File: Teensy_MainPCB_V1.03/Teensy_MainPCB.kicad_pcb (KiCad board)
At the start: 2 copper layers, 141.9 x 100 mm, 62 parts, among them J1 ODO_Right, J10 Sonar_R, J11 Cutter, J12 Sonar_L, J13 P_Right, J15 Button, J16 Power_PCB1, J17 Power_PCB2, J18 Free01_02, J19 P_Left, J2 I2C2_0, J20 Can3, J21 Ser5, J22 FreeA16_A17, J23 ESP RFID1, J24 ESP RFID2, J25 5V IN, J26 ESP32 I2C, J27 ESP32 Sens1, J28 ESP32 FREE, J3 I2C0_0, J30 I2C1_0, J31 Ser3, J32 ESP32 Sens2, J33 ESP32 I2C/SER, J34 Teensy On/Off, J4 I2C1_1, J5 Bumper, J6 ODO_Left, J7 Motor_Right1, J8 Motor_Left1, J9 Rain, U2 GY-521, U3 Teensy4.1, U4 ESP32-DEVKIT-V1

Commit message: v1.03
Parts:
- removed D7: 1N5819, Diode_THT:D_DO-41_SOD81_P10.16mm_Horizontal
- removed J32: ESP32 Sens2, Connector_JST:JST_XH_B3B-XH-A_1x03_P2.50mm_Vertical
- removed J33: ESP32 I2C/SER, Connector_JST:JST_XH_B4B-XH-A_1x04_P2.50mm_Vertical
- removed J34: Teensy On/Off, Connector_JST:JST_XH_B2B-XH-A_1x02_P2.50mm_Vertical
- removed JP3: MotorPower, Connector_PinHeader_2.54mm:PinHeader_1x03_P2.54mm_Vertical
- removed JP5: CutterPower, Connector_PinHeader_2.54mm:PinHeader_1x03_P2.54mm_Vertical
- removed U4: ESP32-DEVKIT-V1, teensy_library-master:ESP32-DEVKIT-V1
- added C1: CP1, Capacitor_THT:CP_Radial_D8.0mm_P3.80mm, F.Cu at (53.5, 119.2)
- added D1: 1N4733A, Diode_THT:D_DO-41_SOD81_P10.16mm_Horizontal, F.Cu at (51.1, 47.1)
- added J14: Button, Connector_JST:JST_XH_B2B-XH-A_1x02_P2.50mm_Vertical, F.Cu at (43.5, 122.4)
- added J29: ESP RFID2, Connector_JST:JST_XH_B5B-XH-A_1x05_P2.50mm_Vertical, F.Cu at (119.7, 117.1)
- added JP1: MotorPower, Connector_PinHeader_2.54mm:PinHeader_1x03_P2.54mm_Vertical, F.Cu at (171.0, 121.7)
- added JP2: CutterPower, Connector_PinHeader_2.54mm:PinHeader_1x03_P2.54mm_Vertical, F.Cu at (171.6, 49.0)
- added R11: XXXX, Resistor_THT:R_Axial_DIN0207_L6.3mm_D2.5mm_P2.54mm_Vertical, F.Cu at (55.5, 38.8)
- added U1: Teensy4.1, teensy_library-master:Teensy41, F.Cu at (69.0, 87.7)
- added kibuzzard-62AA1DDF: G***, kibuzzard-62AA1DDF, F.Cu at (39.4, 111.8)
- added kibuzzard-62AA1E85: G***, kibuzzard-62AA1E85, F.Cu at (53.4, 80.6)
- added kibuzzard-62AA1F05: G***, kibuzzard-62AA1F05, F.Cu at (53.1, 83.2)
- added kibuzzard-62AA3447: G***, kibuzzard-62AA3447, F.Cu at (68.7, 42.2)
- added kibuzzard-62AA347B: G***, kibuzzard-62AA347B, F.Cu at (50.2, 95.9)
- added kibuzzard-62AA34D8: G***, kibuzzard-62AA34D8, F.Cu at (50.2, 98.3)
- added kibuzzard-62AA353C: G***, kibuzzard-62AA353C, F.Cu at (50.2, 100.7)
- added kibuzzard-62AA3566: G***, kibuzzard-62AA3566, F.Cu at (50.2, 103.3)
- added kibuzzard-62AA39DC: G***, kibuzzard-62AA39DC, F.Cu at (39.5, 120.9)
- added kibuzzard-62AA3A43: G***, kibuzzard-62AA3A43, F.Cu at (39.5, 97.2)
- added kibuzzard-62AA3A85: G***, kibuzzard-62AA3A85, F.Cu at (39.4, 81.9)
- added kibuzzard-62AA3B12: G***, kibuzzard-62AA3B12, F.Cu at (39.4, 48.0)
- added kibuzzard-62AB5E06: G***, kibuzzard-62AB5E06, F.Cu at (81.3, 35.6)
- added kibuzzard-62AB5E66: G***, kibuzzard-62AB5E66, F.Cu at (63.0, 35.6)
- added kibuzzard-62AB5ED1: G***, kibuzzard-62AB5ED1, F.Cu at (93.6, 35.6)
- added kibuzzard-62AB5F2F: G***, kibuzzard-62AB5F2F, F.Cu at (102.0, 35.6)
- added kibuzzard-62AB5F67: G***, kibuzzard-62AB5F67, F.Cu at (114.3, 35.6)
- added kibuzzard-62AB5FC4: G***, kibuzzard-62AB5FC4, F.Cu at (129.3, 35.5)
- added kibuzzard-62AB5FF2: G***, kibuzzard-62AB5FF2, F.Cu at (137.7, 35.5)
- added kibuzzard-62AB6021: G***, kibuzzard-62AB6021, F.Cu at (150.9, 35.5)
- added kibuzzard-62AB60B1: G***, kibuzzard-62AB60B1, F.Cu at (90.7, 62.4)
- added kibuzzard-62AB6109: G***, kibuzzard-62AB6109, F.Cu at (90.6, 65.0)
- added kibuzzard-62AB62B6: G***, kibuzzard-62AB62B6, F.Cu at (87.4, 44.7)
- added kibuzzard-62AB62D3: G***, kibuzzard-62AB62D3, F.Cu at (87.5, 47.3)
- added kibuzzard-62AB634F: G***, kibuzzard-62AB634F, F.Cu at (108.2, 44.9)
- added kibuzzard-62AB6374: G***, kibuzzard-62AB6374, F.Cu at (108.2, 47.5)
- added kibuzzard-62AB639B: G***, kibuzzard-62AB639B, F.Cu at (121.8, 44.8)
- added kibuzzard-62AB63D2: G***, kibuzzard-62AB63D2, F.Cu at (121.6, 47.4)
- added kibuzzard-62AB64C2: G***, kibuzzard-62AB64C2, F.Cu at (144.3, 42.2)
- added kibuzzard-62AB64F2: G***, kibuzzard-62AB64F2, F.Cu at (143.9, 47.3)
- added kibuzzard-62AB6557: G***, kibuzzard-62AB6557, F.Cu at (156.3, 44.6)
- added kibuzzard-62AB6A77: G***, kibuzzard-62AB6A77, F.Cu at (84.6, 55.9)
- added kibuzzard-62AB6A93: G***, kibuzzard-62AB6A93, F.Cu at (97.0, 55.8)
- added kibuzzard-62AB6AFA: G***, kibuzzard-62AB6AFA, F.Cu at (90.3, 67.5)
- added kibuzzard-62AB6B3D: G***, kibuzzard-62AB6B3D, F.Cu at (90.3, 70.0)
- added kibuzzard-62AB6B9B: G***, kibuzzard-62AB6B9B, F.Cu at (102.6, 70.0)
- added kibuzzard-62AB6BA8: G***, kibuzzard-62AB6BA8, F.Cu at (102.6, 67.5)
- added kibuzzard-62AB6BF4: G***, kibuzzard-62AB6BF4, F.Cu at (111.6, 55.7)
- added kibuzzard-62AB6CC8: G***, kibuzzard-62AB6CC8, F.Cu at (123.6, 55.6)
- added kibuzzard-62AB6D7A: G***, kibuzzard-62AB6D7A, F.Cu at (114.2, 65.6)
- added kibuzzard-62AB6EF0: G***, kibuzzard-62AB6EF0, F.Cu at (139.4, 55.6)
- added kibuzzard-62AB6F91: G***, kibuzzard-62AB6F91, F.Cu at (142.9, 66.2)
- added kibuzzard-62AB7031: G***, kibuzzard-62AB7031, F.Cu at (174.2, 46.1)
- added kibuzzard-62AB756D: G***, kibuzzard-62AB756D, F.Cu at (154.6, 55.5)
- added kibuzzard-62AB767F: G***, kibuzzard-62AB767F, F.Cu at (173.5, 118.8)
- added kibuzzard-62AB774A: G***, kibuzzard-62AB774A, F.Cu at (167.0, 69.5)
- added kibuzzard-62AB778D: G***, kibuzzard-62AB778D, F.Cu at (178.2, 63.4)
- added kibuzzard-62AB77E5: G***, kibuzzard-62AB77E5, F.Cu at (178.1, 84.4)
- added kibuzzard-62AB789F: G***, kibuzzard-62AB789F, F.Cu at (177.9, 106.4)
- added kibuzzard-62AC4CEE: G***, kibuzzard-62AC4CEE, F.Cu at (153.4, 98.2)
- added kibuzzard-62AC4D6D: G***, kibuzzard-62AC4D6D, F.Cu at (155.7, 88.1)
- added kibuzzard-62AC52F4: G***, kibuzzard-62AC52F4, F.Cu at (96.0, 132.2)
- added kibuzzard-62AC8CBD: G***, kibuzzard-62AC8CBD, F.Cu at (143.4, 39.7)
- added kibuzzard-62AC8CC8: G***, kibuzzard-62AC8CC8, F.Cu at (143.5, 44.9)
- added kibuzzard-62AC8CD7: G***, kibuzzard-62AC8CD7, F.Cu at (156.8, 42.3)
- added kibuzzard-62AC8CE7: G***, kibuzzard-62AC8CE7, F.Cu at (111.6, 66.1)
- added kibuzzard-62AC8CFB: G***, kibuzzard-62AC8CFB, F.Cu at (123.6, 66.1)
- added kibuzzard-62AC8D10: G***, kibuzzard-62AC8D10, F.Cu at (140.3, 66.1)
- added kibuzzard-62AC8D1B: G***, kibuzzard-62AC8D1B, F.Cu at (155.8, 66.1)
- added kibuzzard-62AC8D87: G***, kibuzzard-62AC8D87, F.Cu at (153.2, 88.0)
- added kibuzzard-62AC8DAF: G***, kibuzzard-62AC8DAF, F.Cu at (49.8, 122.8)
- added kibuzzard-62AC8DEE: G***, kibuzzard-62AC8DEE, F.Cu at (50.1, 90.7)
- added kibuzzard-62AC8E7D: G***, kibuzzard-62AC8E7D, F.Cu at (108.1, 42.3)
- added kibuzzard-62AC8E96: G***, kibuzzard-62AC8E96, F.Cu at (121.6, 42.1)
- added kibuzzard-62AC8EE6: G***, kibuzzard-62AC8EE6, F.Cu at (90.7, 59.9)
- added kibuzzard-62AC8F0E: G***, kibuzzard-62AC8F0E, F.Cu at (121.0, 65.6)
- added kibuzzard-62AC8F57: G***, kibuzzard-62AC8F57, F.Cu at (158.3, 66.3)
- added kibuzzard-62AC8F80: G***, kibuzzard-62AC8F80, F.Cu at (135.3, 66.5)
- added kibuzzard-62AC8F92: G***, kibuzzard-62AC8F92, F.Cu at (150.9, 66.6)
- added kibuzzard-62AC8FB5: G***, kibuzzard-62AC8FB5, F.Cu at (126.1, 65.8)
- added kibuzzard-62AC8FDD: G***, kibuzzard-62AC8FDD, F.Cu at (137.8, 65.7)
- added kibuzzard-62AC8FEE: G***, kibuzzard-62AC8FEE, F.Cu at (153.3, 65.8)
- added kibuzzard-62AC90B9: G***, kibuzzard-62AC90B9, F.Cu at (150.7, 87.6)
- added kibuzzard-62AC90FB: G***, kibuzzard-62AC90FB, F.Cu at (69.1, 39.6)
- added kibuzzard-62AC9112: G***, kibuzzard-62AC9112, F.Cu at (157.2, 39.7)
- added kibuzzard-62AC9161: G***, kibuzzard-62AC9161, F.Cu at (167.8, 62.0)
- added kibuzzard-62AC916E: G***, kibuzzard-62AC916E, F.Cu at (167.7, 83.1)
- added kibuzzard-62AC917A: G***, kibuzzard-62AC917A, F.Cu at (167.6, 105.0)
- added kibuzzard-62AC918B: G***, kibuzzard-62AC918B, F.Cu at (167.7, 64.5)
- added kibuzzard-62AC9196: G***, kibuzzard-62AC9196, F.Cu at (167.7, 85.8)
- added kibuzzard-62AC91A3: G***, kibuzzard-62AC91A3, F.Cu at (167.5, 107.6)
- added kibuzzard-62AC91BB: G***, kibuzzard-62AC91BB, F.Cu at (168.2, 67.0)
- added kibuzzard-62AC91C5: G***, kibuzzard-62AC91C5, F.Cu at (168.1, 88.3)
- added kibuzzard-62AC91DF: G***, kibuzzard-62AC91DF, F.Cu at (167.9, 110.1)
- added kibuzzard-62AC91F0: G***, kibuzzard-62AC91F0, F.Cu at (166.7, 112.6)
- added kibuzzard-62AC9203: G***, kibuzzard-62AC9203, F.Cu at (166.7, 90.8)
- added kibuzzard-62AC92C8: G***, kibuzzard-62AC92C8, F.Cu at (49.8, 93.4)
- added kibuzzard-62AC9315: G***, kibuzzard-62AC9315, F.Cu at (69.0, 44.9)
- added kibuzzard-62AC932E: G***, kibuzzard-62AC932E, F.Cu at (69.1, 47.4)
- added kibuzzard-62AC9376: G***, kibuzzard-62AC9376, F.Cu at (109.0, 65.7)
- added kibuzzard-62AC93D0: G***, kibuzzard-62AC93D0, F.Cu at (87.6, 42.3)
- added kibuzzard-62AC95A7: G***, kibuzzard-62AC95A7, F.Cu at (167.6, 59.3)
- added kibuzzard-62AC95BD: G***, kibuzzard-62AC95BD, F.Cu at (167.6, 80.6)
- added kibuzzard-62AC95C9: G***, kibuzzard-62AC95C9, F.Cu at (167.5, 102.5)
- added kibuzzard-62AC961B: G***, kibuzzard-62AC961B, F.Cu at (87.5, 39.7)
- added kibuzzard-62AC9630: G***, kibuzzard-62AC9630, F.Cu at (108.2, 39.9)
- added kibuzzard-62AC9639: G***, kibuzzard-62AC9639, F.Cu at (121.6, 39.6)
- J1: value ODO_Right -> 5V IN; footprint Connector_JST:JST_XH_B4B-XH-A_1x04_P2.50mm_Vertical -> TerminalBlock:TerminalBlock_bornier-2_P5.08mm
- J10: value Sonar_R -> P_Right; footprint Connector_JST:JST_XH_B4B-XH-A_1x04_P2.50mm_Vertical -> Connector_JST:JST_XH_B3B-XH-A_1x03_P2.50mm_Vertical
- J11: value Cutter -> I2C1_1; footprint Connector_JST:JST_XH_B5B-XH-A_1x05_P2.50mm_Vertical -> Connector_JST:JST_XH_B4B-XH-A_1x04_P2.50mm_Vertical
- J12: value Sonar_L -> I2C0_0
- J13: value P_Right -> I2C1_0; footprint Connector_JST:JST_XH_B3B-XH-A_1x03_P2.50mm_Vertical -> Connector_JST:JST_XH_B4B-XH-A_1x04_P2.50mm_Vertical
- J15: value Button -> Power_PCB1; footprint Connector_JST:JST_XH_B2B-XH-A_1x02_P2.50mm_Vertical -> Connector_JST:JST_XH_B6B-XH-A_1x06_P2.50mm_Vertical
- J16: value Power_PCB1 -> Power_PCB2; footprint Connector_JST:JST_XH_B6B-XH-A_1x06_P2.50mm_Vertical -> Connector_JST:JST_XH_B2B-XH-A_1x02_P2.50mm_Vertical
- J17: value Power_PCB2 -> FreeA17; footprint Connector_JST:JST_XH_B2B-XH-A_1x02_P2.50mm_Vertical -> Connector_JST:JST_XH_B3B-XH-A_1x03_P2.50mm_Vertical
- J18: value Free01_02 -> Teensy On/Off; footprint Connector_JST:JST_XH_B3B-XH-A_1x03_P2.50mm_Vertical -> Connector_JST:JST_XH_B2B-XH-A_1x02_P2.50mm_Vertical
- J19: value P_Left -> Ser3; footprint Connector_JST:JST_XH_B3B-XH-A_1x03_P2.50mm_Vertical -> Connector_JST:JST_XH_B5B-XH-A_1x05_P2.50mm_Vertical
- J20: value Can3 -> ESP RFID1
- J21: value Ser5 -> ESP32 Sens1; footprint Connector_JST:JST_XH_B5B-XH-A_1x05_P2.50mm_Vertical -> Connector_JST:JST_XH_B3B-XH-A_1x03_P2.50mm_Vertical
- J22: value FreeA16_A17 -> ESP32 Sens2; footprint Connector_JST:JST_XH_B4B-XH-A_1x04_P2.50mm_Vertical -> Connector_JST:JST_XH_B3B-XH-A_1x03_P2.50mm_Vertical
- J23: value ESP RFID1 -> ESP32 FREE; footprint Connector_JST:JST_XH_B5B-XH-A_1x05_P2.50mm_Vertical -> Connector_JST:JST_XH_B4B-XH-A_1x04_P2.50mm_Vertical
- J24: value ESP RFID2 -> Ser5
- J25: value 5V IN -> Can3; footprint TerminalBlock:TerminalBlock_bornier-2_P5.08mm -> Connector_JST:JST_XH_B5B-XH-A_1x05_P2.50mm_Vertical
- J26: value ESP32 I2C -> Motor_Right; footprint Connector_JST:JST_XH_B4B-XH-A_1x04_P2.50mm_Vertical -> Connector_JST:JST_XH_B6B-XH-A_1x06_P2.50mm_Vertical
- J27: value ESP32 Sens1 -> Motor_Left; footprint Connector_JST:JST_XH_B3B-XH-A_1x03_P2.50mm_Vertical -> Connector_JST:JST_XH_B6B-XH-A_1x06_P2.50mm_Vertical
- J28: value ESP32 FREE -> ESP32 I2C/SER
- J3: value I2C0_0 -> Rain; footprint Connector_JST:JST_XH_B4B-XH-A_1x04_P2.50mm_Vertical -> Connector_JST:JST_XH_B3B-XH-A_1x03_P2.50mm_Vertical
- J30: value I2C1_0 -> ESP32 I2C
- J31: value Ser3 -> Cutter; footprint Connector_JST:JST_XH_B5B-XH-A_1x05_P2.50mm_Vertical -> Connector_JST:JST_XH_B6B-XH-A_1x06_P2.50mm_Vertical
- J4: value I2C1_1 -> Bumper
- J5: value Bumper -> Sonar_L
- J7: value Motor_Right1 -> ODO_Right; footprint Connector_JST:JST_XH_B5B-XH-A_1x05_P2.50mm_Vertical -> Connector_JST:JST_XH_B4B-XH-A_1x04_P2.50mm_Vertical
- J8: value Motor_Left1 -> Sonar_R; footprint Connector_JST:JST_XH_B5B-XH-A_1x05_P2.50mm_Vertical -> Connector_JST:JST_XH_B4B-XH-A_1x04_P2.50mm_Vertical
- J9: value Rain -> P_Left
- R1, R3: value XXXX -> 2KO
- R10, R8: value 2KO -> 1KO
- R12: value 2KO -> 1k/100 Ohm
- R13: value 2KO -> XXX
- R14, R15, R2, R4: value XXX -> 2KO
- R16, R17: value 1.5KO -> 1KO
- R18, R19, R6: value 1KO -> XXX
- R5: value 1KO -> XXXX
- U3: value Teensy4.1 -> ESP32-DEVKIT-V1; footprint teensy_library-master:Teensy41 -> teensy_library-master:ESP32-DEVKIT-V1
- moved J1 122.4 mm to (44.5, 45.4)
- moved R12 117.2 mm to (51.1, 53.1), turned to 90 degrees
- moved R5 116.6 mm to (57.7, 46.0), turned to 180 degrees
- moved J17 107.7 mm to (150.7, 93.3), turned to 0 degrees
- moved J30 97.6 mm to (137.9, 126.3), turned to 0 degrees
- moved J18 93.1 mm to (43.6, 112.9), turned to 90 degrees
- moved J31 92.5 mm to (174.1, 56.9)
- moved R13 86.3 mm to (75.9, 39.3), turned to 180 degrees
- moved J3 84.2 mm to (151.6, 39.6)
- moved R6 83.7 mm to (75.8, 47.0), turned to 180 degrees
- moved J25 82.9 mm to (54.0, 128.1), turned to 0 degrees
- moved R1 82.8 mm to (138.6, 70.4)
- moved J11 82.4 mm to (94.2, 39.8)
- moved R2 82.4 mm to (154.0, 70.5)
- moved J21 79.4 mm to (152.5, 112.6), turned to 0 degrees
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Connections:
- J1 pad 1: Net-(J1-Pad1) -> GND
- J1 pad 2: GND -> Net-(J1-Pad2)
- J10 pad 1: +3V3 -> +5V
- J10 pad 3: pinSonarRightTrigger -> Net-(J10-Pad3)
- J11 pad 1: Net-(J11-Pad1) -> +3V3
- J11 pad 3: pinMotorMowPWM -> SDA1
- J11 pad 4: pinMotorMowDir -> SCL1
- J12 pad 3: pinSonarLeftTrigger -> SDA0
- J12 pad 4: pinSonarLeftEcho -> SCL0
- J13 pad 1: +5V -> +3V3
- J13 pad 3: Net-(J13-Pad3) -> SDA1
- J15 pad 1: GND -> SCL1
- J15 pad 2: pinButton -> SDA1
- J16 pad 1: SCL1 -> pinChargeEnable
- J16 pad 2: SDA1 -> pinBatterySwitch
- J17 pad 1: pinChargeEnable -> +3V3
- J17 pad 2: pinBatterySwitch -> GND
- J18 pad 1: GND -> Net-(J18-Pad1)
- J18 pad 2: Free01 -> Net-(J18-Pad2)
- J19 pad 2: GND -> +3V3
- J19 pad 3: Net-(J19-Pad3) -> GND
- J20 pad 1: +5V -> GND
- J20 pad 2: +3V3 -> +5V
- J20 pad 3: GND -> Net-(J20-Pad3)
- J20 pad 4: CTX3 -> Net-(J20-Pad4)
- J20 pad 5: CRX3 -> Net-(J20-Pad5)
- J21 pad 2: +3V3 -> GND
- J21 pad 3: GND -> Net-(J21-Pad3)
- J22 pad 1: +3V3 -> +5V
- J22 pad 3: FreeA16 -> Net-(J22-Pad3)
- J23 pad 1: GND -> Net-(J23-Pad1)
- J23 pad 2: +5V -> Net-(J23-Pad2)
- J24 pad 1: Net-(J24-Pad1) -> +5V
- J24 pad 2: Net-(J24-Pad2) -> +3V3
- J24 pad 3: Net-(J24-Pad3) -> GND
- J24 pad 4: Net-(J24-Pad4) -> TX5
- J24 pad 5: unconnected-(J24-Pad5) -> RX5
- J25 pad 1: GND -> +5V
- J25 pad 2: Net-(D7-Pad2) -> +3V3
- J26 pad 1: GND -> Net-(J26-Pad1)
- J26 pad 2: Net-(J26-Pad2) -> GND
- J26 pad 3: Net-(J26-Pad3) -> pinMotorRightPWM
- J26 pad 4: Net-(J24-Pad4) -> pinMotorRightDir
- J27 pad 1: +5V -> Net-(J26-Pad1)
- J27 pad 3: Net-(J27-Pad3) -> pinMotorLeftPWM
- J3 pad 3: SDA0 -> pinRain
- J30 pad 1: +3V3 -> GND
- J30 pad 2: GND -> Net-(J30-Pad2)
- J30 pad 3: SDA1 -> Net-(J30-Pad3)
- J30 pad 4: SCL1 -> Net-(J29-Pad4)
- J31 pad 1: +5V -> Net-(J31-Pad1)
- J31 pad 2: +3V3 -> GND
- J31 pad 3: GND -> pinMotorMowPWM
- J31 pad 4: TX3 -> pinMotorMowDir
- J31 pad 5: RX3 -> pinMotorMowEnable
- J4 pad 1: +3V3 -> GND
- J4 pad 2: GND -> pinBumperRight
- J4 pad 3: SDA1 -> GND
- J4 pad 4: SCL1 -> pinBumperLeft
- J5 pad 1: GND -> +3V3
- J5 pad 2: pinBumperRight -> GND
- J5 pad 3: GND -> pinSonarLeftTrigger
- J5 pad 4: pinBumperLeft -> pinSonarLeftEcho
- J7 pad 3: pinMotorRightPWM -> +5V
- J7 pad 4: pinMotorRightDir -> +3V3
- J8 pad 1: Net-(J7-Pad1) -> +3V3
- J8 pad 3: pinMotorLeftPWM -> pinSonarRightTrigger
- J8 pad 4: pinMotorLeftDir -> pinSonarRightEcho
- J9 pad 1: +3V3 -> +5V
- J9 pad 3: pinRain -> Net-(J9-Pad3)
- R1 pad 1: SCL0 -> GND
- R1 pad 2: +3V3 -> pinOdometryLeft
- R10 pad 1: pinPerimeterLeft -> pinPerimeterRight
- R10 pad 2: GND -> Net-(J10-Pad3)
- R12 pad 1: GND -> Net-(J1-Pad2)
- R12 pad 2: pinOdometryRight -> +5V
- R13 pad 1: GND -> SDA1
- R13 pad 2: pinOdometryLeft -> +3V3
- R14 pad 1: Net-(J24-Pad4) -> Net-(J21-Pad3)
- R14 pad 2: Net-(J26-Pad2) -> GND
- R15 pad 1: Net-(J24-Pad4) -> Net-(J22-Pad3)
- R15 pad 2: Net-(J26-Pad3) -> GND
- R16 pad 1: Net-(J27-Pad3) -> Net-(J21-Pad3)
- R16 pad 2: GND -> Net-(R16-Pad2)
- R17 pad 1: Net-(J32-Pad3) -> Net-(J22-Pad3)
- R17 pad 2: GND -> Net-(R17-Pad2)
- R18 pad 1: Net-(J27-Pad3) -> Net-(J29-Pad4)
- R18 pad 2: Net-(R18-Pad2) -> Net-(J30-Pad2)
- R19 pad 1: Net-(J32-Pad3) -> Net-(J29-Pad4)
- R19 pad 2: Net-(R19-Pad2) -> Net-(J30-Pad3)
- R2 pad 1: SCL1 -> GND
- R2 pad 2: +3V3 -> pinOdometryRight
- R3 pad 1: +3V3 -> pinPerimeterLeft
- R3 pad 2: SDA0 -> GND
- R4 pad 1: SDA1 -> pinPerimeterRight
- R4 pad 2: +3V3 -> GND
- R5 pad 1: Net-(J1-Pad1) -> SCL0
- R5 pad 2: pinOdometryRight -> +3V3
- R6 pad 1: Net-(J6-Pad1) -> SCL1
- R6 pad 2: pinOdometryLeft -> +3V3
- R7 pad 1: Net-(J13-Pad3) -> pinOdometryLeft
- R7 pad 2: pinPerimeterRight -> Net-(J6-Pad1)
- R8 pad 1: pinPerimeterRight -> pinOdometryRight
- R8 pad 2: GND -> Net-(J7-Pad1)
- R9 pad 1: Net-(J19-Pad3) -> pinPerimeterLeft
- R9 pad 2: pinPerimeterLeft -> Net-(J9-Pad3)
- U3 pad 1: GND -> unconnected-(U3-Pad1)
- U3 pad 10: pinMotorMowEnable -> unconnected-(U3-Pad10)
- U3 pad 11: pinMotorMowDir -> Net-(J20-Pad5)
- U3 pad 12: pinMotorMowPWM -> Net-(J20-Pad4)
- U3 pad 13: pinOdometryRight -> Net-(J20-Pad3)
- U3 pad 14: pinOdometryLeft -> GND
- U3 pad 15: +3V3 -> +5V
- U3 pad 16: SCL2 -> Net-(J29-Pad4)
- U3 pad 17: SDA2 -> GND
- U3 pad 18: pinSonarLeftEcho -> Net-(J30-Pad2)
- U3 pad 19: pinSonarRightEcho -> unconnected-(U3-Pad19)
- U3 pad 2: RX1 -> unconnected-(U3-Pad2)
- U3 pad 20: pinSonarLeftTrigger -> Net-(J30-Pad3)
- U3 pad 21: pinSonarRightTrigger -> TX1
- U3 pad 22: CRX3 -> RX1
- U3 pad 23: CTX3 -> unconnected-(U3-Pad23)
- U3 pad 24: Free02 -> Net-(J29-Pad3)
- U3 pad 25: pinBatterySwitch -> Net-(J29-Pad2)
- U3 pad 26: pinChargeEnable -> Net-(J28-Pad3)
- U3 pad 27: pinBumperLeft -> Net-(J28-Pad2)
- U3 pad 28: pinBumperRight -> Net-(J28-Pad1)
- U3 pad 29: pinBuzzer -> Net-(J28-Pad4)
- U3 pad 3: TX1 -> unconnected-(U3-Pad3)
- U3 pad 30: pinButton -> Net-(J29-Pad1)
- U3 pad 4: pinMotorRightEnable -> Net-(R16-Pad2)
- U3 pad 5: pinMotorRightDir -> Net-(R17-Pad2)
- U3 pad 6: pinMotorRightPWM -> Net-(J23-Pad4)
- U3 pad 7: pinMotorLeftEnable -> Net-(J23-Pad3)
- U3 pad 8: pinMotorLeftDir -> Net-(J23-Pad2)
- U3 pad 9: pinMotorLeftPWM -> Net-(J23-Pad1)
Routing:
- net GND: track 664.5 -> 345.0 mm
- net pinMotorRightBreak: track 0.00 -> 175.3 mm, vias 0 -> 1
- net pinMotorLeftBreak: track 0.00 -> 154.4 mm
- net pinMotorMowBreak: track 0.00 -> 132.2 mm
- net Net-(R19-Pad2): track 106.2 -> 0.00 mm
- net Net-(R18-Pad2): track 101.4 -> 0.00 mm
- net Free01: track 96.2 -> 0.00 mm, vias 1 -> 0
- net FreeA16: track 95.2 -> 0.00 mm, vias 1 -> 0
- net Net-(R17-Pad2): track 0.00 -> 92.7 mm
- net Net-(R16-Pad2): track 0.00 -> 77.9 mm
- net Free02: track 74.0 -> 0.00 mm, vias 1 -> 0
- net Net-(J23-Pad2): track 0.00 -> 70.8 mm
- net Net-(J23-Pad1): track 0.00 -> 68.4 mm
- net +5V: track 350.9 -> 418.9 mm
- net Net-(J18-Pad2): track 0.00 -> 66.7 mm
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- removed copper zone on F.Cu, net GND
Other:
- board text removed: "+3.3V"
- board text removed: "A16"
- board text removed: "A17"
- board text removed: "BatterySwitch"
- board text removed: "ChargeEnable"
- board text removed: "DIR"
- board text removed: "EN"
- board text removed: "Echo"
- board text removed: "F01"
- board text removed: "F02"
- board text removed: "IN"
- board text removed: "Left"
- board text removed: "PWM"
- board text removed: "RX3"
- board text removed: "RX5"
- board text removed: "Right"
- board text removed: "SCL0"
- board text removed: "SCL1"
- board text removed: "SCL2"
- board text removed: "SDA0"
- board text removed: "SDA1"
- board text removed: "SDA2"
- board text removed: "SIG"
- board text removed: "TX3"
- board text removed: "TX5"
- board text removed: "Teensy MainPCB V1.03"
- board text removed: "Trigger"

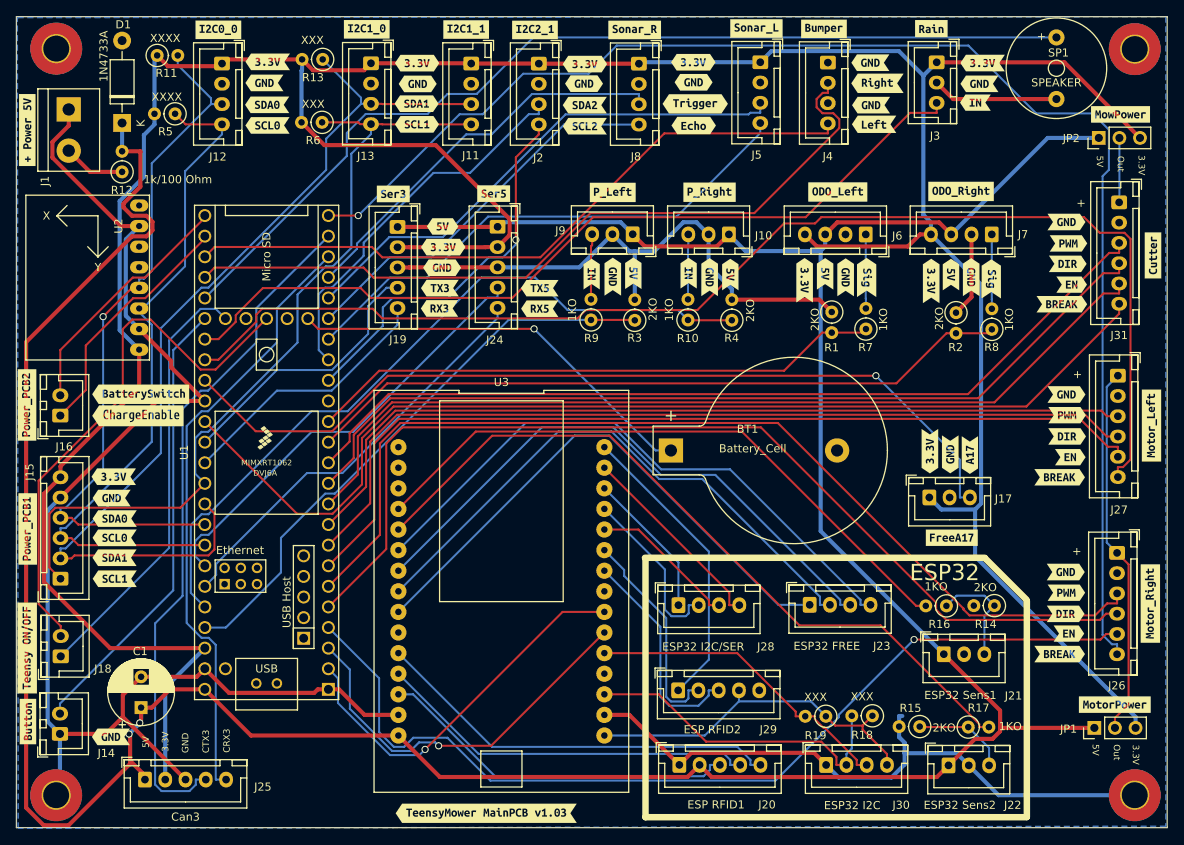
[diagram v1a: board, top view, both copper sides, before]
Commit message: Rework of chargePCB
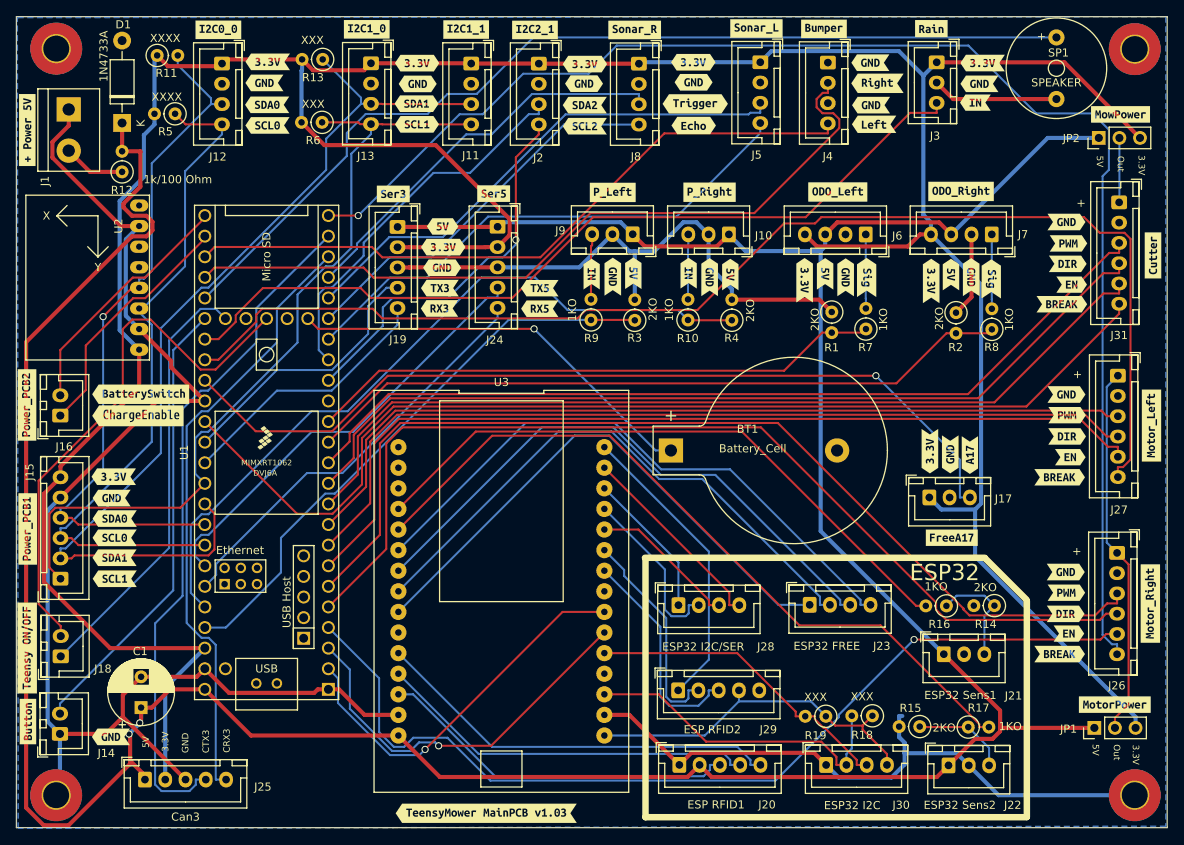
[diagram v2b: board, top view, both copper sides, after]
